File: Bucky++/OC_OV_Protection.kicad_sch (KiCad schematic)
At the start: 66 parts, among them IC10 TPS259830ONRGER, IC7 TPS259830ONRGER, IC8 TPS259830ONRGER, IC9 TPS259830ONRGER, Q9 RS1E260ATTB1, U4 ADM1270ACPZ

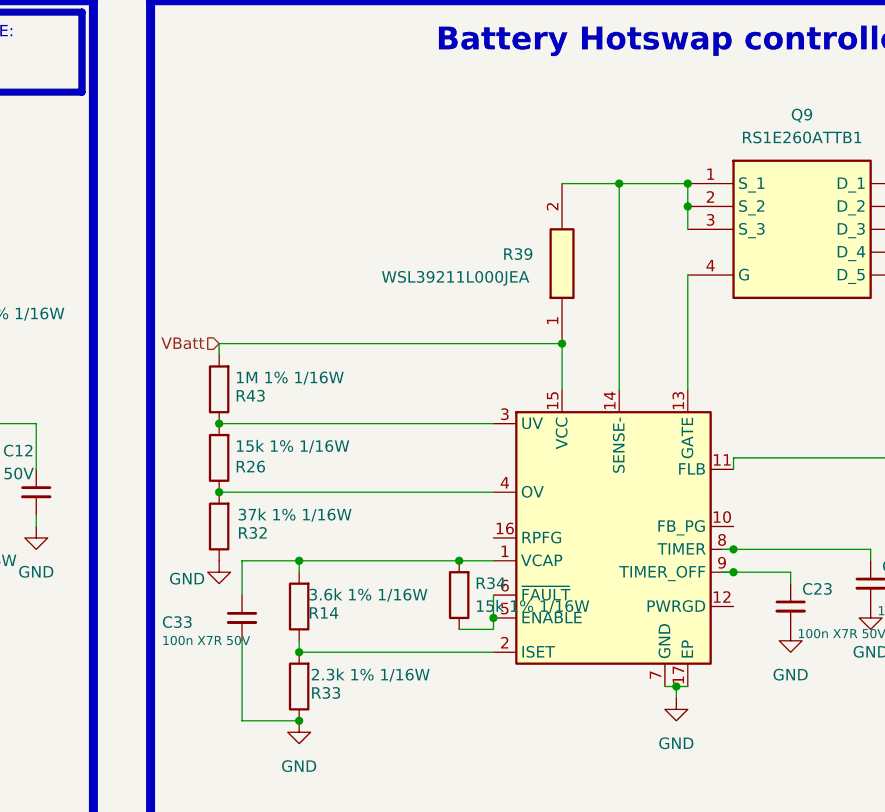
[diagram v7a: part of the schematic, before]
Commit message: wider planes, USB impedance matching
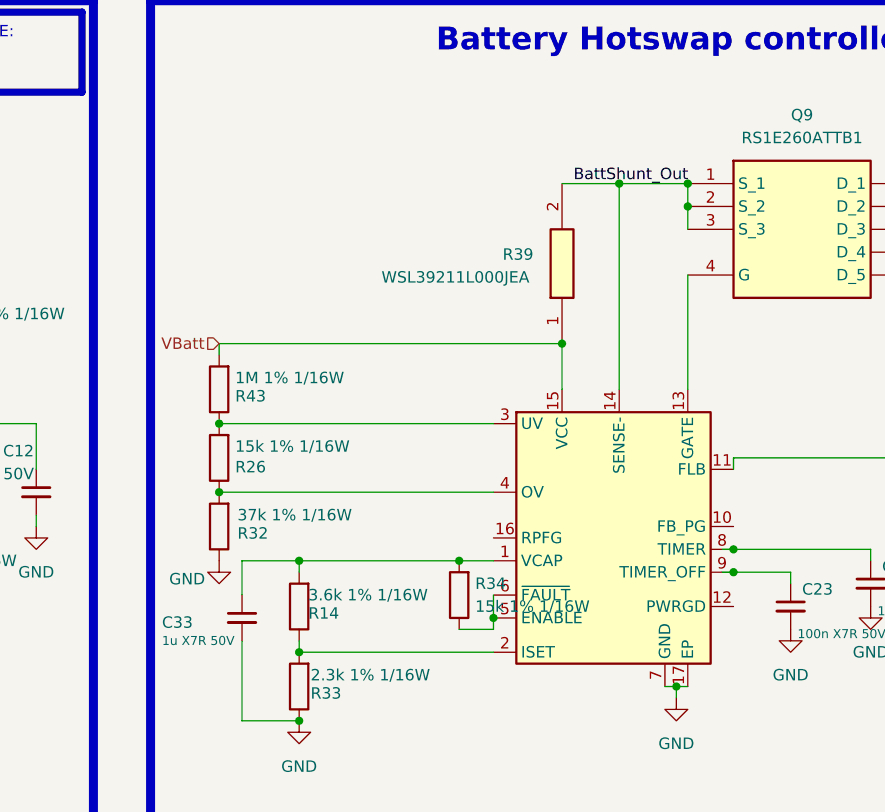
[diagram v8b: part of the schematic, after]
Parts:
- C33: value 100n X7R 50V -> 1u X7R 50V
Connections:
- net BattShunt_Out: now reaches Q9.1 (S_1), Q9.2 (S_2), Q9.3 (S_3), R39.2, U4.14 (SENSE-)
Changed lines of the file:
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@@
+		)
+	)
+	(label "BattShunt_Out"
+		(at 308.61 63.5 0)
+		(effects
+			(font
+				(size 1.27 1.27)
+			)
+			(justify left bottom)
 		)
 	)
@@
 			)
 		)
-		(property "Value" "100n X7R 50V"
+		(property "Value" "1u X7R 50V"
 			(at 262.89 114.3 0)
 			(effects
